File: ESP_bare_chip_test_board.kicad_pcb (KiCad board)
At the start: 4 copper layers, 57.1 x 63.5 mm, 131 parts, among them J1201 NorComp - 112-024-113RYY1, J1301 Conn_01x06, J1302 Conn_01x06, J1501 Conn_01x04, J1502 Conn_01x04, J201 Conn_01x06, J501 Barrel_Jack, J502 PWR_IN, J503 ALTERNATE, J801 USB_C_Receptacle, J802 USB_C_Receptacle, Q301 40MHz, Q501 DTC114E, Q502 DTC114E, Q701 40MHz, SW201 SW_Push, SW202 SW_Push, U1001 TLV62569DBV, U1002 TPS63070, U1401 W25Q128JVS, U1501 D1213A-04TS-7, U301 W25Q128JVS, U302 ESP32-S3, U501 TPS2552DBV, U502 TPS2552DBV, U701 W25Q128JVS, U702 ESP32-S3, U801 D1213A-04TS-7, U802 D1213A-04TS-7, U803 FUSB302BPX

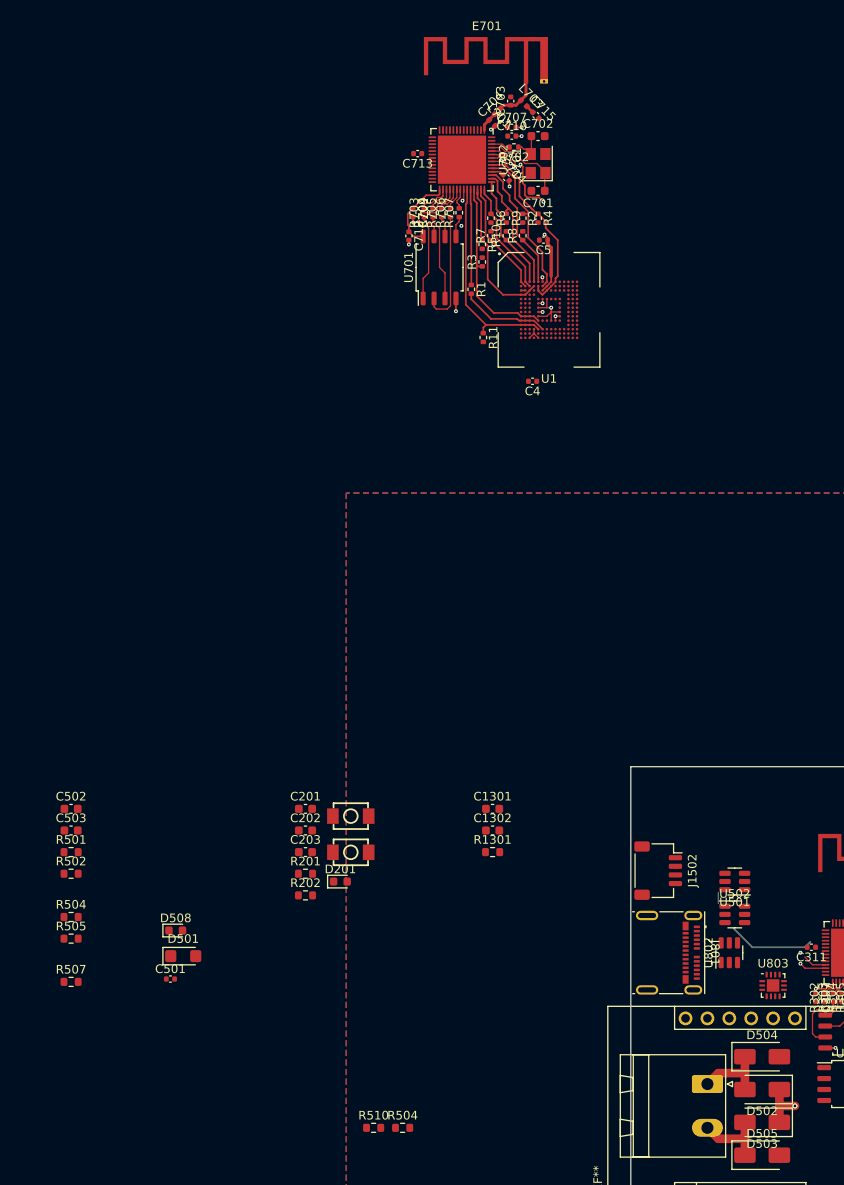
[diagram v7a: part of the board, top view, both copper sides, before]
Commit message: Removed USB-PD circuit - simplifies board
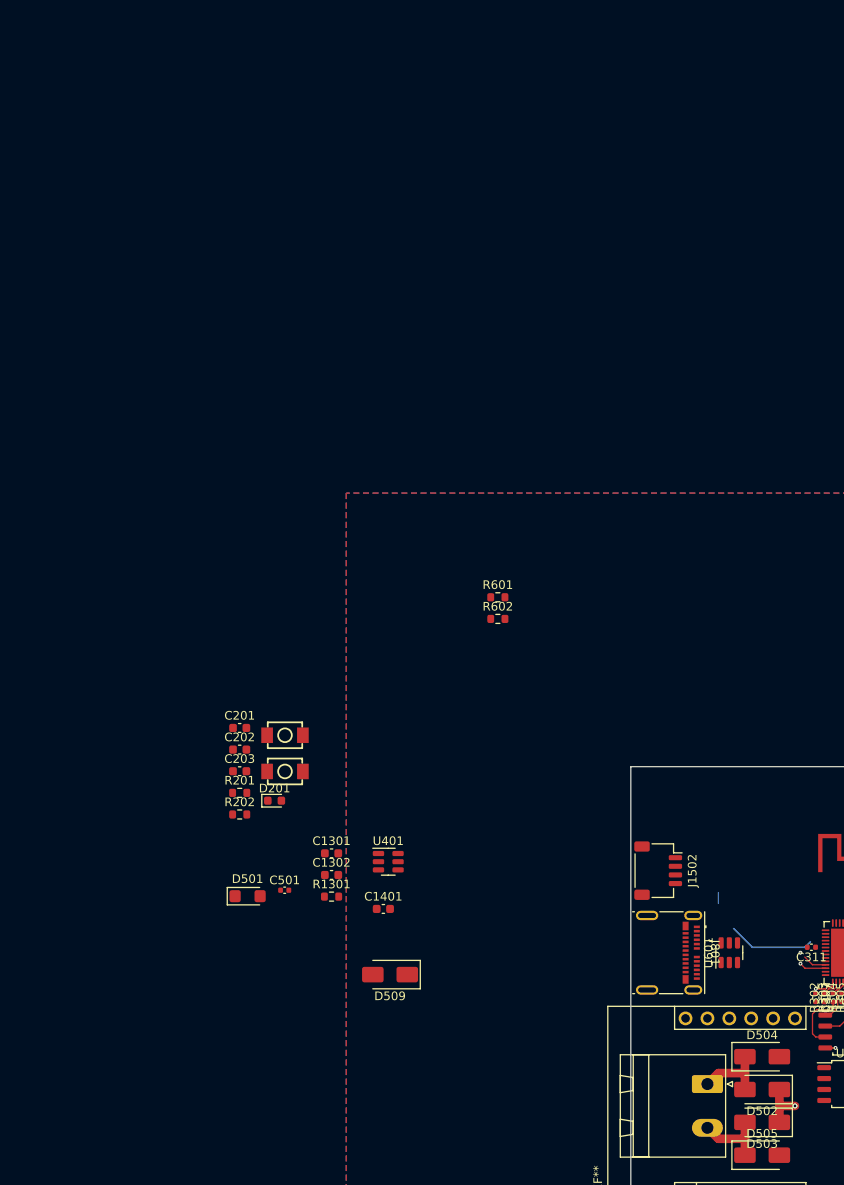
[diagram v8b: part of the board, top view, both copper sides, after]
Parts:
- removed C4: 2.2uF, Capacitor_SMD:C_0402_1005Metric
- removed C5, C712, C713, C714: 0.1uF, Capacitor_SMD:C_0402_1005Metric
- removed C502, C503: 100nF/50V, Capacitor_SMD:C_0603_1608Metric
- removed C701, C702: 10pF, Capacitor_SMD:C_0603_1608Metric
- removed C703: 2.7pF, Capacitor_SMD:C_0402_1005Metric
- removed C704: 4.7pF, Capacitor_SMD:C_0402_1005Metric
- removed C707, C709: 1uF, Capacitor_SMD:C_0402_1005Metric
- removed C710: 10nF, Capacitor_SMD:C_0402_1005Metric
- removed C715: TBD, Capacitor_SMD:C_0402_1005Metric
- removed D508: YELLOW, LED_SMD:LED_0603_1608Metric
- removed E701: ANTENNA-GROUNDEDTRACE-15.2MM, RF_Antenna_custom:Texas_SWRA117D_2.4GHz_Left
- removed L701: 1.6nH, Inductor_SMD:L_0402_1005Metric
- removed L703: TBD, Inductor_SMD:L_0402_1005Metric
- removed Q701: 40MHz, Crystal:Crystal_SMD_3225-4Pin_3.2x2.5mm
- removed R1: 22Ω, Resistor_SMD:R_0402_1005Metric
- removed R10, R2, R3, R4, R5, R6, R7, R8, R9: 50kΩ, Resistor_SMD:R_0402_1005Metric
- removed R11: 10kΩ, Resistor_SMD:R_0402_1005Metric
- removed R501, R505: 15kΩ/1%, Resistor_SMD:R_0603_1608Metric
- removed R502, R510: 100kΩ, Resistor_SMD:R_0603_1608Metric
- removed R504: 10kΩ, Resistor_SMD:R_0603_1608Metric
- removed R504: 33kΩ, Resistor_SMD:R_0603_1608Metric
- removed R507: 15kΩ, Resistor_SMD:R_0603_1608Metric
- removed R702: TBD, 24nH to start, Resistor_SMD:R_0402_1005Metric
- removed R703, R704, R705, R706, R707: 0, Resistor_SMD:R_0402_1005Metric
- removed U1: ~, Package_BGA_custom:FBGA-153_11.5x13mm_Layout14x14_P0.5mm_Ball0.3_Pad0.3mm_NSMD
- removed U501, U502: TPS2552DBV, Package_TO_SOT_SMD:SOT-23-6
- removed U701: W25Q128JVS, Package_SO:SOIC-8_5.23x5.23mm_P1.27mm
- removed U702: ESP32-S3, Package_DFN_QFN:QFN-56-1EP_7x7mm_P0.4mm_EP5.6x5.6mm
- removed U802: D1213A-04TS-7, Package_TO_SOT_SMD:TSOT-23-6
- removed U803: FUSB302BPX, Package_DFN_QFN:WQFN-14-1EP_2.5x2.5mm_P0.5mm_EP1.45x1.45mm
- added C1401: 100nF/50V, Capacitor_SMD:C_0603_1608Metric, F.Cu at (85.6, 63.5)
- added D509: SS210, Diode_SMD:D_SMA, F.Cu at (86.4, 71.1)
- added R601: 5.1k, Resistor_SMD:R_0603_1608Metric, F.Cu at (98.9, 27.3)
- added R602: 5.1k, Resistor_SMD:R_0603_1608Metric, F.Cu at (98.9, 29.8)
- added U401: MASWSS0179, Package_TO_SOT_SMD:SOT-23-6, F.Cu at (86.2, 58.0)
- added U601: D1213A-04TS-7, Package_TO_SOT_SMD:TSOT-23-6, F.Cu at (125.7, 68.6)
- moved C1301 19.4 mm to (79.6, 57.0)
- moved C1302 19.4 mm to (79.6, 59.6)
- moved R1301 19.4 mm to (79.6, 62.1)
- moved C501 16.8 mm to (74.1, 61.3)
- moved SW201 12.1 mm to (74.2, 43.3)
- moved SW202 12.1 mm to (74.2, 47.5)
- moved C202 12.1 mm to (68.9, 45.0)
- moved D201 12.1 mm to (73.0, 50.9)
- moved C201 12.1 mm to (68.9, 42.5)
- moved C203 12.1 mm to (68.9, 47.5)
- moved R201 12.1 mm to (68.9, 50.0)
- moved R202 12.1 mm to (68.9, 52.5)
- moved D501 10.2 mm to (69.8, 62.0)
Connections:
- net /Power/buck-boost-5v/V_{AUS} renamed /Power/buck-boost-5v/V_{AUX}
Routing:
- net (no net): track 145.2 -> 2.27 mm, vias 31 -> 10
- net /ESP32-S3/IO17: track 24.1 -> 0.00 mm
- net /ESP32-S3/IO42: track 24.7 -> 3.09 mm
- net /USB_D-: track 24.2 -> 2.79 mm
- net /ESP32-S3/IO41: track 19.3 -> 1.27 mm
- net /USB_D+: track 22.1 -> 4.40 mm
- net /ESP32-S3/ESP32-S3-core/VDD_SPI: track 28.9 -> 15.2 mm
- net /ESP32-S3/IO26: track 13.4 -> 0.00 mm
- net /ESP32-S3/IO21: track 13.4 -> 0.00 mm
- net /ESP32-S3/IO18: track 11.1 -> 0.00 mm
- net Net-(U302-XTAL_N): track 19.5 -> 9.90 mm
- net /ESP32-S3/ESP32-S3-core/SPID: track 16.5 -> 7.29 mm
- net +3V3: track 10.1 -> 6.07 mm
- net Net-(C302-Pad1): track 7.75 -> 3.87 mm
- net /ESP32-S3/IO14: track 3.06 -> 0.00 mm
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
